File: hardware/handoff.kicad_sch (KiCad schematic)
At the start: 67 parts, among them J1 BAT XH-2, J2 PAD JST-XH 2p, J3 LED JST-XH 4p / 5mm RGB, J5 CHG XH-2, SW1 SS-12F23G5, SW2 TACT 6x6, U1 Raspberry Pi Pico 2 W, U2 MCP6292-E/MS

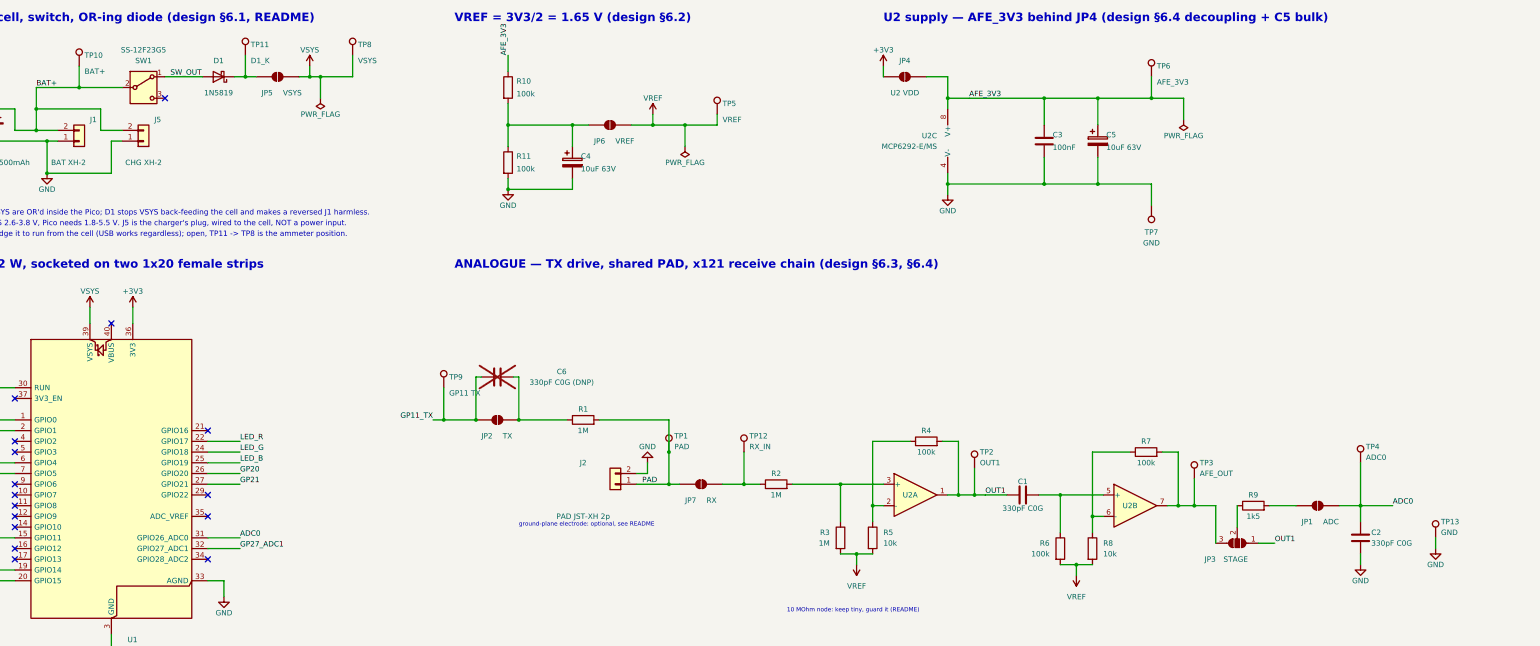
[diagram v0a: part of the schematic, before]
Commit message: Remove all thirteen test pads, and re-lay the elbow block
Each test pad sat on the same net as a solder-jumper pad, a connector pin or a
Pico header pin a couple of millimetres away, and this board is probed with a
meter or a scope tip rather than a clip, so every one of them was a duplicate
occupying through-hole space in the two places the board had none.

Five were in the elbow jumper block, which had eleven parts in 12 x 13 mm:
three gaps of 0.9 mm across it and none at all down the sides. With six parts
it re-lays as two columns 2.96 mm apart with a corridor between them. R10 is
flipped end for end so its two links become single hops instead of crossing.

65 footprints to 52, and 17 unconnected items to 3. The three that remain are
all behind OUT1's descent on the right-hand side; the README says what would
clear them. No shorts, no crossings, no clearance violations, parity still 0.

Costs JP5's ammeter position: board current now means holding a meter across
JP5's own 1 x 0.5 mm pads.

Co-Authored-By: Claude Opus 5 <noreply@anthropic.com>
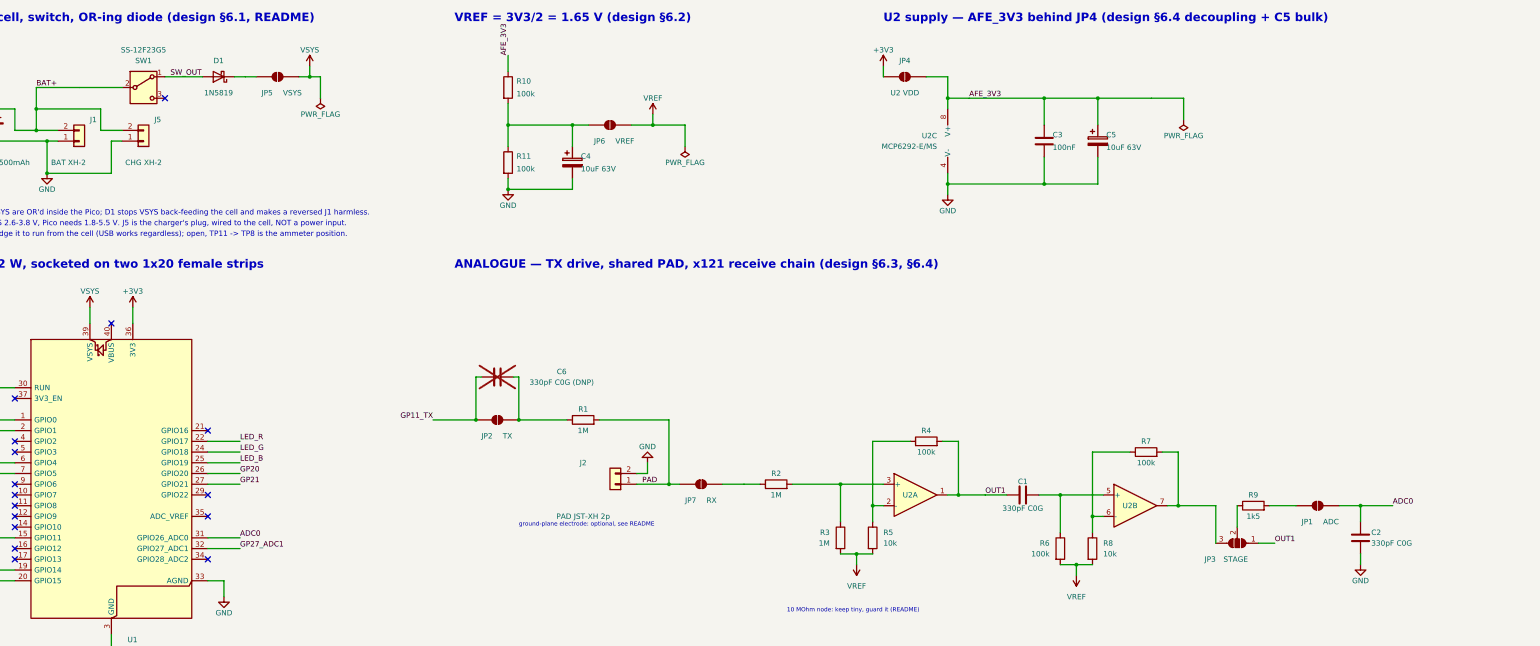
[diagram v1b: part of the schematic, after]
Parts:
- removed TP1: PAD, TestPoint:TestPoint_Pad_D1.5mm, symbol Connector:TestPoint
- removed TP10: BAT+, TestPoint:TestPoint_Pad_D1.5mm, symbol Connector:TestPoint
- removed TP11: D1_K, TestPoint:TestPoint_Pad_D1.5mm, symbol Connector:TestPoint
- removed TP12: RX_IN, TestPoint:TestPoint_Pad_D1.5mm, symbol Connector:TestPoint
- removed TP13, TP7: GND, TestPoint:TestPoint_Pad_D1.5mm, symbol Connector:TestPoint
- removed TP2: OUT1, TestPoint:TestPoint_Pad_D1.5mm, symbol Connector:TestPoint
- removed TP3: AFE_OUT, TestPoint:TestPoint_Pad_D1.5mm, symbol Connector:TestPoint
- removed TP4: ADC0, TestPoint:TestPoint_Pad_D1.5mm, symbol Connector:TestPoint
- removed TP5: VREF, TestPoint:TestPoint_Pad_D1.5mm, symbol Connector:TestPoint
- removed TP6: AFE_3V3, TestPoint:TestPoint_Pad_D1.5mm, symbol Connector:TestPoint
- removed TP8: VSYS, TestPoint:TestPoint_Pad_D1.5mm, symbol Connector:TestPoint
- removed TP9: GP11 TX, TestPoint:TestPoint_Pad_D1.5mm, symbol Connector:TestPoint

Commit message: Make schematic UUIDs deterministic, fix the Power net class, add TP1-TP7
Random UUIDs meant every gen_schematic.py run rewrote every junction,
wire and symbol path even when nothing changed; they are now uuid5,
seeded from a counter, so the diff is the change.

The Power net class the README documented was never landing in
handoff.kicad_pro: pcbnew.BOARD.Save() rewrites that file from the
blank project the board was built under, so gen_pcb.py's own save
undid gen_schematic.py's write on every run. The net-class table now
lives once, in NET_CLASSES/net_settings(), and gen_pcb.py re-applies
it after Save() via apply_board_settings(). A Rail class (0.4 mm) is
added for +3V3/AFE_3V3, sized to what their lanes actually hold.

DRC severities are tightened: silk, text, connection and courtesy
checks that were warnings are now errors, and two new rules forbid
right-angle corners and stub track segments.

Adds TP1-TP7, the test pads from the layout brief's priority list
(GND, ADC0, OUT1, VREF, PAD, and the VSYS/D1_K ammeter pair), each a
through-hole TestPoint pad wired into EXPECTED_NETS so the board's
parity check covers them too.

Co-Authored-By: Claude Sonnet 5 <noreply@anthropic.com>
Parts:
- added TP1: GND, TestPoint:TestPoint_THTPad_D1.5mm_Drill0.7mm, symbol Connector:TestPoint
- added TP2: ADC0, TestPoint:TestPoint_THTPad_D1.5mm_Drill0.7mm, symbol Connector:TestPoint
- added TP3: OUT1, TestPoint:TestPoint_THTPad_D1.5mm_Drill0.7mm, symbol Connector:TestPoint
- added TP4: VREF, TestPoint:TestPoint_THTPad_D1.5mm_Drill0.7mm, symbol Connector:TestPoint
- added TP5: PAD, TestPoint:TestPoint_THTPad_D1.5mm_Drill0.7mm, symbol Connector:TestPoint
- added TP6: VSYS, TestPoint:TestPoint_THTPad_D1.5mm_Drill0.7mm, symbol Connector:TestPoint
- added TP7: D1_K, TestPoint:TestPoint_THTPad_D1.5mm_Drill0.7mm, symbol Connector:TestPoint
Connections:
- net ADC0: now also TP2.1
- net GND: now also TP1.1
- net OUT1: now also TP3.1
- net PAD: now also TP5.1
- net VREF: now also TP4.1
- net VSYS: now also TP6.1
- net D1_K: now reaches D1.1 (K), JP5.1 (A)
- net D1_K: now also TP7.1
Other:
- note added: "JP5 ships OPEN: bridge it to run from the cell (USB works regardless); open, TP7 -> TP6 is the ammeter position."
- note added: "TP1-TP7 TEST PADS — bring-up order (README)"
- note added: "TP5 loads a 10 MOhm node through R1: a 10x probe or better, never a meter. TP6/TP7 straddle JP5: the ammeter position. AFE_3V3 is probed on C5's + lead."
- note removed: "JP5 ships OPEN: bridge it to run from the cell (USB works regardless); open, TP11 -> TP8 is the ammeter position."

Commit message: Add the haptic motor, move the passives to 0603/0805, unstick the breakout pads
Three changes to the parts order, and one bug they surfaced.

The motor. A 10 mm coin motor (M1, off-board on leads into J6) switched
low-side by an AO3400A (Q1) from GP28, with a 100 R gate series (R16), a
100 k gate pull-down (R17, so the gate cannot float through BOOTSEL) and a
SOD-123 Schottky (D3) across the motor. It runs from VSYS, not the Pico's
3V3: 100 mA of pulsed motor current has no business on the rail that feeds
AFE_3V3 through JP4. The block sits on the bottom face at the thumb end of
the elbow, two millimetres from VSYS at pin 39 and a pour away from the AFE.
D3 has no SKU yet - it is the one part here not already on order.

The passives. 100 k, 10 k and the LED series resistors (now 100 R, not
330 R) are 0603; C4 and C5 are 0805 MLCC instead of 5 mm radial
electrolytics. 1 M, 1k5 and the C0G/X7R capacitors stay 1206 - they were not
re-ordered. Every 0603 pad moved 0.64 mm inward, which walked twenty-odd
track ends off their pads, so ROUTES now names pads - P("R6", "1") - and
gen_pcb.py resolves them against the placed footprint. The shift also closed
the 0.25 mm pour channel under R5 that is the AFE pour's only way out to the
electrode; R5 moved back 0.64 mm and VREF leaves its pad along the pad row
now. C4 and C5 changed face: their feeds were always on the bottom and
reached them through the electrolytics' leads.

The bug. E3, E4 and E10 broke out Pico pins 1, 2 and 3 at x 31.44, which put
their pads 3.3 mm from H4's centre - inside the 8 mm enclosure boss. DRC
missed it because the boss keep-out allows pads (the hole's own NPTH pad is
in the middle of it) and because the "bare pads have no body" rule excused
the courtyard overlap from either side. Both are fixed: report() checks every
pad against every boss circle, and the courtyard exemption no longer applies
against a mounting hole. Regression-tested. The breakouts are now GP3 (5),
GP22 (29) and GND (8); GP0 and GP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
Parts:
- removed H1: M3, handoff:MountingHole_3.4mm_M3_Boss8mm, symbol Mechanical:MountingHole
- added D3: 1N5819W, Diode_SMD:D_SOD-123, symbol Device:D_Schottky
- added H4: M3, handoff:MountingHole_3.4mm_M3_Boss8mm, symbol Mechanical:MountingHole
- added J6: MOT 1x02 2.54, Connector_PinHeader_2.54mm:PinHeader_1x02_P2.54mm_Vertical, symbol Connector_Generic:Conn_01x02
- added M1: 1034 coin 10mm 3V, symbol Motor:Motor_DC
- added Q1: AO3400A, Package_TO_SOT_SMD:SOT-23, symbol Transistor_FET:AO3400A
- added R15: 10k, Resistor_SMD:R_0603_1608Metric_Pad0.98x0.95mm_HandSolder, symbol Device:R
- added R16: 100, Resistor_SMD:R_0603_1608Metric_Pad0.98x0.95mm_HandSolder, symbol Device:R
- added R17: 100k, Resistor_SMD:R_0603_1608Metric_Pad0.98x0.95mm_HandSolder, symbol Device:R
- C4, C5: value 10uF 63V -> 10uF 100V; footprint Capacitor_THT:CP_Radial_D5.0mm_P2.50mm -> Capacitor_SMD:C_0805_2012Metric_Pad1.18x1.45mm_HandSolder; symbol Device:C_Polarized -> Device:C
- E10: value GND (pin 3) -> GND (pin 8)
- E3: value GP0 (pin 1) -> GP3 (pin 5)
- E4: value GP1 (pin 2) -> GP22 (pin 29)
- R10, R11, R4, R5, R6, R7, R8: footprint Resistor_SMD:R_1206_3216Metric_Pad1.30x1.75mm_HandSolder -> Resistor_SMD:R_0603_1608Metric_Pad0.98x0.95mm_HandSolder
- R12, R13, R14: value 330 -> 100; footprint Resistor_SMD:R_1206_3216Metric_Pad1.30x1.75mm_HandSolder -> Resistor_SMD:R_0603_1608Metric_Pad0.98x0.95mm_HandSolder
- TP8: renamed from R15; value 10k -> AFE_3V3; footprint Resistor_SMD:R_1206_3216Metric_Pad1.30x1.75mm_HandSolder -> TestPoint:TestPoint_THTPad_D1.5mm_Drill0.7mm; symbol Device:R -> Connector:TestPoint; now left out of the parts list
- renumbered H2 to H1, H3 to H2, H4 to H3
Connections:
- net +3V3: now also R15.1; no longer TP8.1
- net AFE_3V3: now also TP8.1
- net BTN: now also R15.2; no longer TP8.2
- net GND: now also Q1.2 (S), R17.2
- net VSYS: now also D3.1 (K), J6.2 (Pin_2), M1.1 (+)
- net GP22: now reaches U1.29 (GPIO22)
- net GP22: now also E4.1
- net MOT_DRV: now reaches U1.34 (GPIO28_ADC2)
- net MOT_DRV: now also R16.1
- net GP3: now reaches U1.5 (GPIO3)
- net GP3: now also E3.1
- net GP0: no longer names the net of U1.1 (GPIO0)
- net GP0: no longer E3.1
- net GP1: no longer names the net of U1.2 (GPIO1)
- net GP1: no longer E4.1
- new net: Q1.1 (G), R16.2, R17.1
- new net MOT_SW: D3.2 (A), J6.1 (Pin_1), M1.2 (-), Q1.3 (D)
- no-connect marks 16 -> 15
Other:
- note added: "(M1 drawn for reference: it is the motor whose leads go into J6, not a board component.) D3 is the flyback path: without it the"
- note added: "HAPTIC — 10 mm coin motor on VSYS, low-side AO3400A, gate on GP28"
- note added: "TP1-TP8 TEST PADS — bring-up order (README)"
- note added: "TP5 loads a 10 MOhm node through R1: a 10x probe or better, never a meter. TP6/TP7 straddle JP5: the ammeter position."
- note added: "TP8 is new: C4 and C5 are 0805 MLCC now, so the through-hole + lead that used to be the AFE_3V3 probe point is gone."
- note added: "motor's collapse drives Q1's drain well above VSYS at every turn-off. Firmware: GP28 high runs the motor - never during an RX window."
- note removed: "TP1-TP7 TEST PADS — bring-up order (README)"
- note removed: "TP5 loads a 10 MOhm node through R1: a 10x probe or better, never a meter. TP6/TP7 straddle JP5: the ammeter position. AFE_3V3 is probed on C5's + lead."
- moved on the sheet: H1, H2, H3

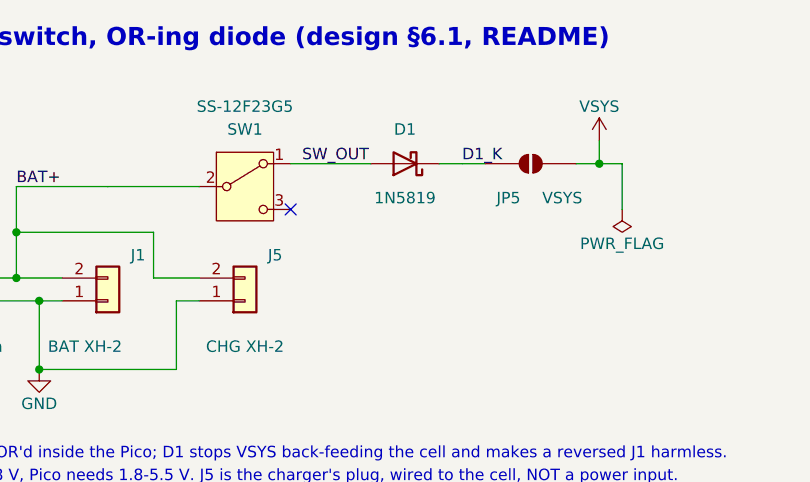
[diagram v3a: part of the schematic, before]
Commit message: Move D1 to the SS220F Schottky (SMB); D3 stays SOD-123
D1 and D3 were both candidates for a single SS220F (Slkor, 200 V 2 A,
SMB/DO-214AA) SKU to replace their 1N5819 parts. D1 took the swap: its
THT DO-41 pads used to be copper on both faces, so its approach tracks
just ended on the pad; SMD is F.Cu only, so each track's existing 45
degree bend became a via with a short F.Cu stub into the pad, and the
oversized SMB body outline moved off silk to stop it clipping TP7.

D3 does not fit: the motor block is a 6 x 9 mm pocket already holding
J6, Q1, R16 and R17, and SMB's courtyard swallowed J6's pad, hung off
the board edge, and clipped two neighbours' solder mask. Left as
1N5819W/SOD-123 pending a decision on a smaller-package Schottky or a
new location for it.

Co-Authored-By: Claude Sonnet 5 <noreply@anthropic.com>
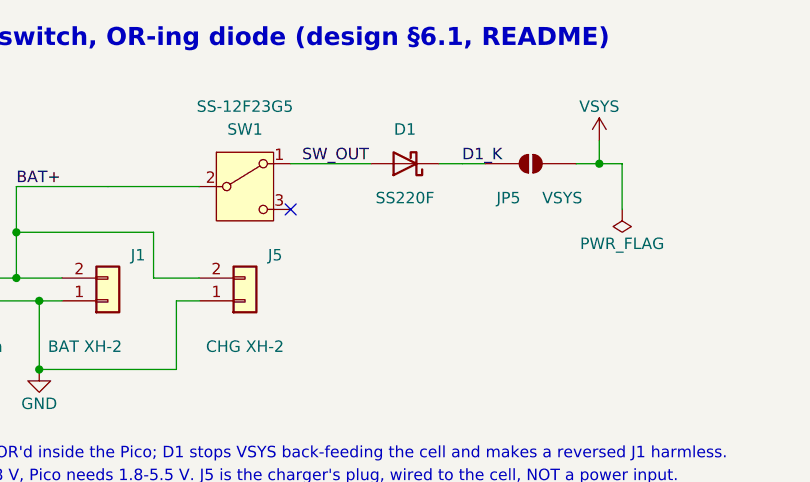
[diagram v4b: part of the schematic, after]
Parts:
- D1: value 1N5819 -> SS220F; footprint Diode_THT:D_DO-41_SOD81_P7.62mm_Horizontal -> Diode_SMD:D_SMB
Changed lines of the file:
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@@
 			)
 		)
-		(property "Value" "1N5819"
+		(property "Value" "SS220F"
 			(at 83.8200 34.2900 0)
 			(effects
@@
 			)
 		)
-		(property "Footprint" "Diode_THT:D_DO-41_SOD81_P7.62mm_Horizontal"
+		(property "Footprint" "Diode_SMD:D_SMB"
 			(at 83.8200 30.4800 0)
 			(effects
@@
 			)
 		)
-		(property "Description" "VSYS OR-ing / reverse polarity"
+		(property "Description" "VSYS OR-ing / reverse polarity, Schottky 200 V 2 A, SMB"
 			(at 83.8200 30.4800 0)
 			(effects
